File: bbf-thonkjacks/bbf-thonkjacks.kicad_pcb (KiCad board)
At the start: 2 copper layers, 20.3 x 52.1 mm, 7 parts, among them J1 WQP-PJ301M-12_JACK, J2 WQP-PJ301M-12_JACK, J3 WQP-PJ301M-12_JACK, J4 WQP-PJ301M-12_JACK

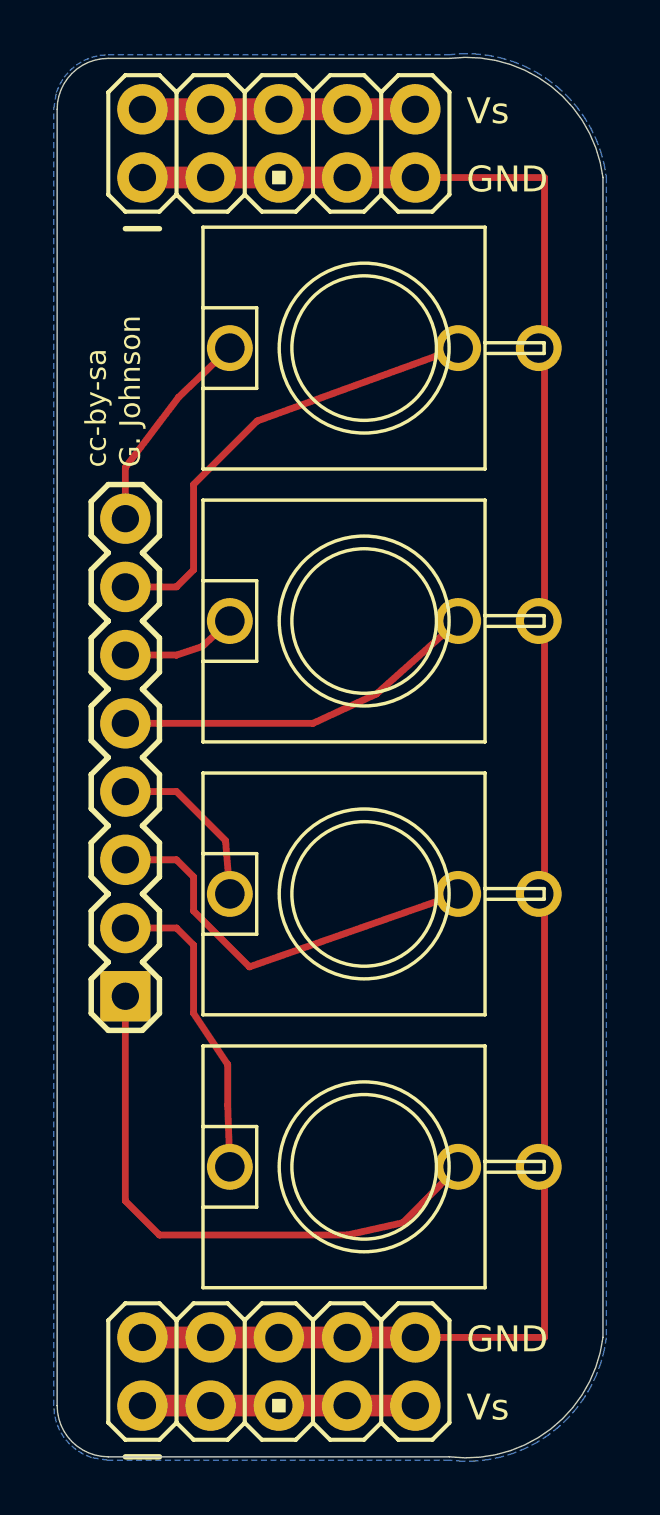
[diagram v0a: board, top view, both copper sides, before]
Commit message: Update bbf-thonkjacks jack footprint
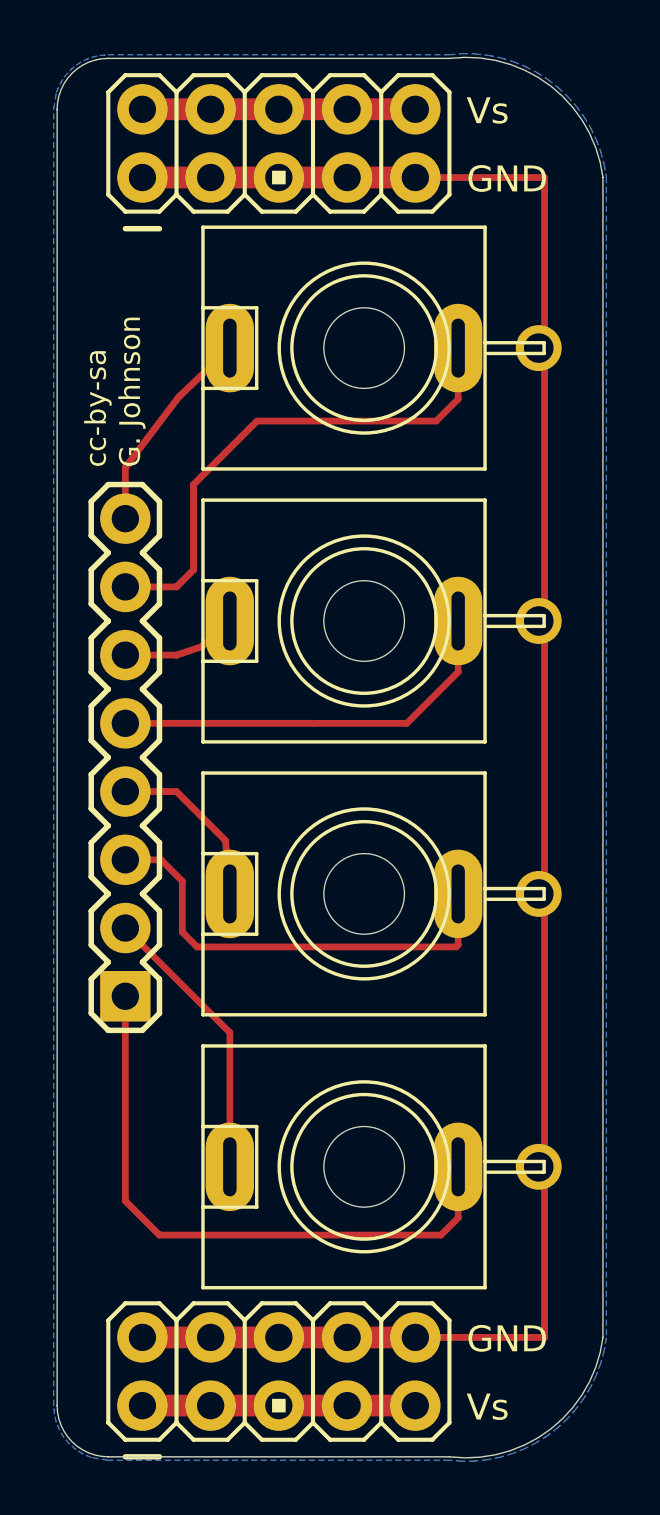
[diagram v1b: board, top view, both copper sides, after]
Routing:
- net Net-(J1-PadP$2): track 17.3 -> 19.0 mm
- net Net-(J3-PadP$2): track 15.2 -> 16.8 mm
- net Net-(J2-PadP$2): track 13.7 -> 15.1 mm
- net Net-(J4-PadP$2): track 21.5 -> 22.7 mm
- net Net-(J4-PadP$1): track 11.4 -> 10.5 mm
